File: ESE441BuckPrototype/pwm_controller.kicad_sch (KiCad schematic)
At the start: 56 parts, among them IC1 NCP81233MNTXG, J1 Header

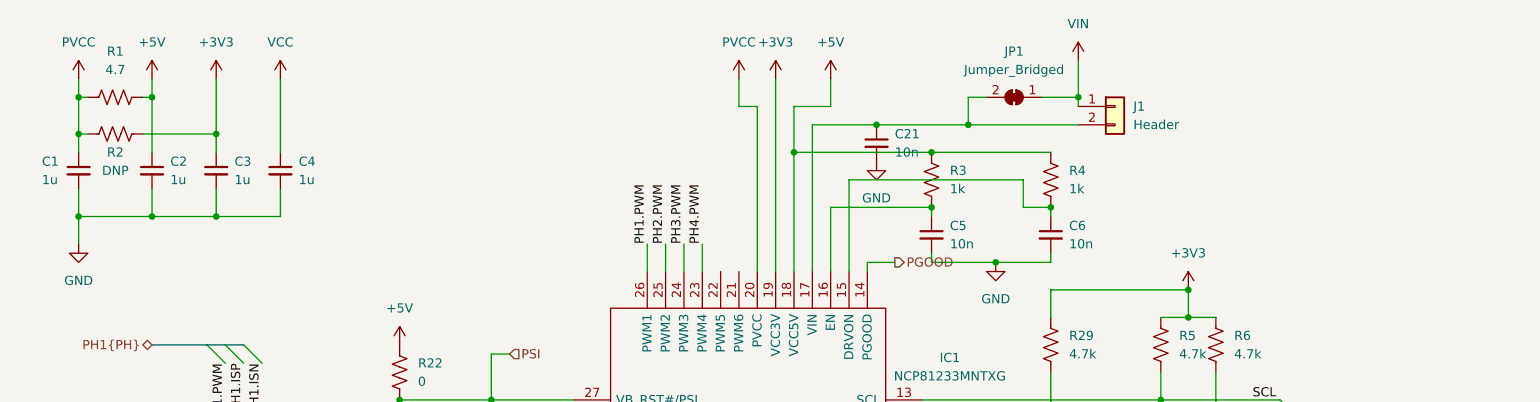
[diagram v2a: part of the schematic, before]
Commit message: Connect enable to MCU; Testpoints
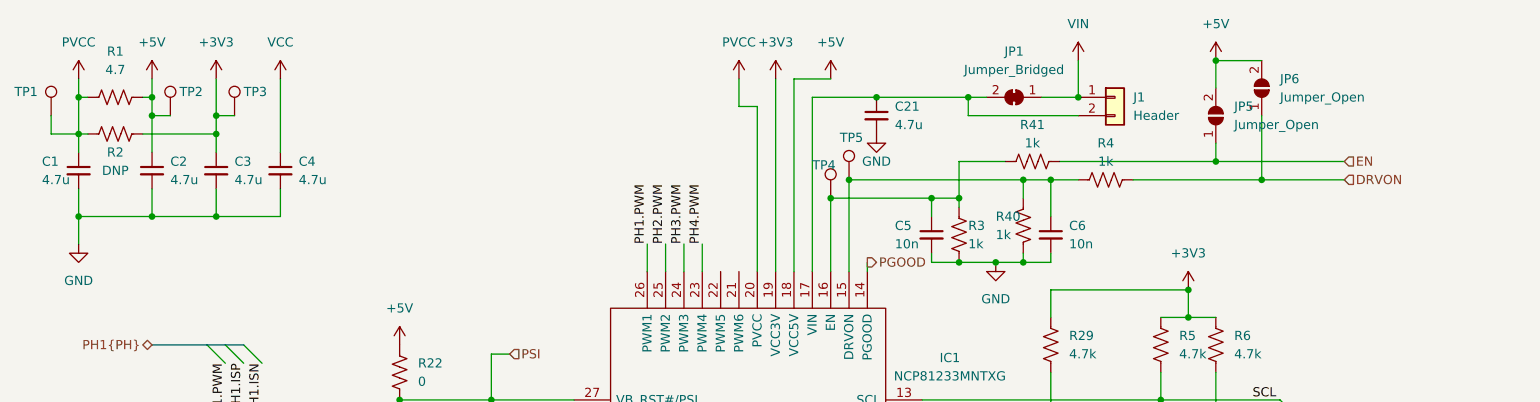
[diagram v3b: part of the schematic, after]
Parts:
- added JP5, JP6: Jumper_Open, symbol Jumper:SolderJumper_2_Open
- added R40, R41: 1k, Resistor_SMD:R_0603_1608Metric, symbol Device:R_US
- added TP1, TP2, TP3, TP4, TP5: TestPoint, TestPoint:TestPoint_Loop_D2.50mm_Drill1.0mm_LowProfile, symbol Connector:TestPoint
- C1, C2, C3, C4: value 1u -> 4.7u
- C21: value 10n -> 4.7u
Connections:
- net +3V3: now also TP3.1
- net +5V: now also JP5.2 (B), JP6.2 (B), TP2.1; no longer R3.1, R4.1
- net GND: now also R3.1, R40.2
- net PVCC: now also TP1.1
- net at C6.1, IC1.15 (DRVON), R4.2: now also R40.1, TP5.1
- net at C5.1, IC1.16 (EN), R3.2: now also R41.2, TP4.1
- new net DRVON: JP6.1 (A), R4.1
- new net EN: JP5.1 (A), R41.1
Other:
- moved on the sheet: C21, J1, R3, R4

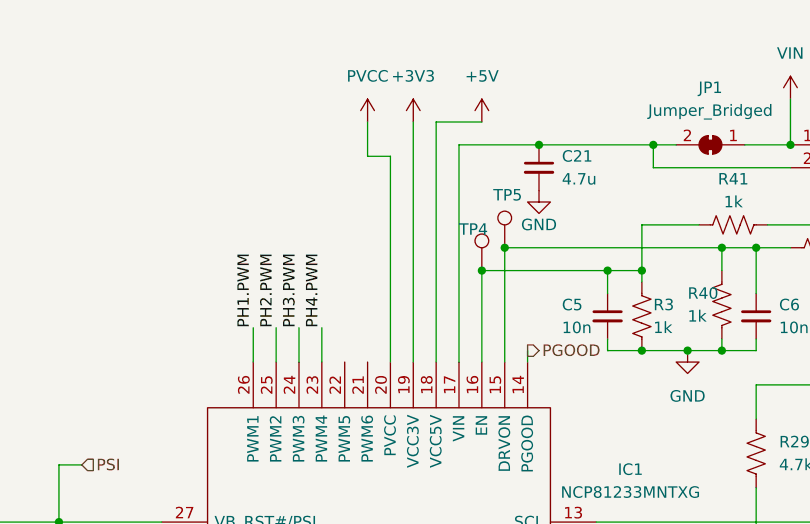
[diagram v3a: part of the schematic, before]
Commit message: Add openable jumper for internal 5V LDO
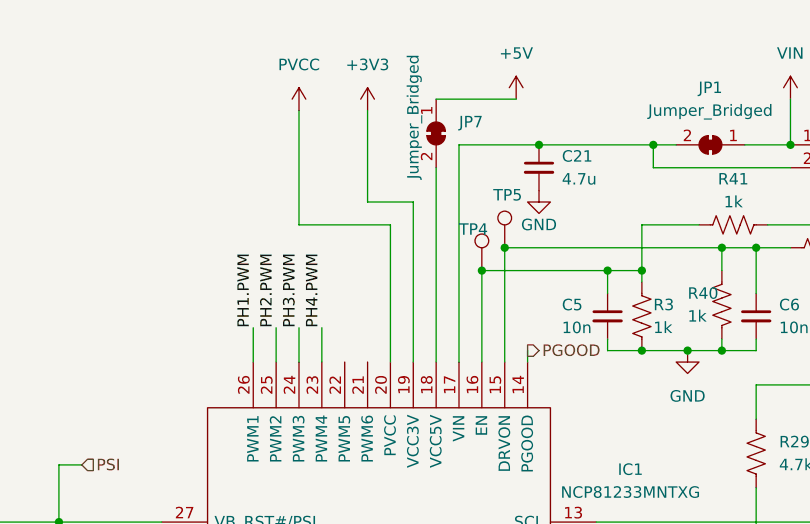
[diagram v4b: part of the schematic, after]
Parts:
- added JP7: Jumper_Bridged, symbol Jumper:SolderJumper_2_Bridged
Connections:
- net +5V: now also JP7.1 (A); no longer IC1.18 (VCC5V)
- new net: IC1.18 (VCC5V), JP7.2 (B)
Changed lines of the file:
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@@
-    (stroke (width 0) (type default) (color 0 0 0 0))
-  )
-  (wire (pts (xy 128.27 24.13) (xy 123.19 24.13))
     (stroke (width 0) (type default) (color 0 0 0 0))
   )
@@
     (stroke (width 0) (type default) (color 0 0 0 0))
   )
-  (wire (pts (xy 120.65 24.13) (xy 120.65 50.8))
-    (stroke (width 0) (type default) (color 0 0 0 0))
-  )
   (bus (pts (xy 193.04 71.12) (xy 195.58 71.12))
     (stroke (width 0) (type default) (color 0 0 0 0))
   )
+  (wire (pts (xy 115.57 22.86) (xy 115.57 33.02))
+    (stroke (width 0) (type default) (color 0 0 0 0))
+  )
   (wire (pts (xy 182.88 88.9) (xy 140.97 88.9))
     (stroke (width 0) (type default) (color 0 0 0 0))
@@
     (stroke (width 0) (type default) (color 0 0 0 0))
   )
+  (wire (pts (xy 118.11 35.56) (xy 107.95 35.56))
+    (stroke (width 0) (type default) (color 0 0 0 0))
+  )
   (wire (pts (xy 190.5 68.58) (xy 173.99 68.58))
     (stroke (width 0) (type default) (color 0 0 0 0))
@@
     (stroke (width 0) (type default) (color 0 0 0 0))
   )
+  (wire (pts (xy 107.95 35.56) (xy 107.95 22.86))
+    (stroke (width 0) (type default) (color 0 0 0 0))
+  )
   (wire (pts (xy 81.28 153.67) (xy 76.2 153.67))
     (stroke (width 0) (type default) (color 0 0 0 0))
@@
     (stroke (width 0) (type default) (color 0 0 0 0))
   )
-  (wire (pts (xy 115.57 24.13) (xy 115.57 27.94))
-    (stroke (width 0) (type default) (color 0 0 0 0))
-  )
   (wire (pts (xy 76.2 129.54) (xy 76.2 140.97))
     (stroke (width 0) (type default) (color 0 0 0 0))
@@
     (stroke (width 0) (type default) (color 0 0 0 0))
   )
+  (wire (pts (xy 123.19 21.59) (xy 132.08 21.59))
+    (stroke (width 0) (type default) (color 0 0 0 0))
+  )
+  (wire (pts (xy 115.57 33.02) (xy 120.65 33.02))
+    (stroke (width 0) (type default) (color 0 0 0 0))
+  )
   (bus (pts (xy 34.29 101.6) (xy 41.91 101.6))
     (stroke (width 0) (type default) (color 0 0 0 0))
@@
     (stroke (width 0) (type default) (color 0 0 0 0))
   )
+  (wire (pts (xy 120.65 33.02) (xy 120.65 50.8))
+    (stroke (width 0) (type default) (color 0 0 0 0))
+  )
   (wire (pts (xy 149.86 132.08) (xy 163.83 132.08))
     (stroke (width 0) (type default) (color 0 0 0 0))
@@
     (stroke (width 0) (type default) (color 0 0 0 0))
   )
+  (wire (pts (xy 123.19 29.21) (xy 123.19 50.8))
+    (stroke (width 0) (type default) (color 0 0 0 0))
+  )
   (wire (pts (xy 196.85 107.95) (xy 204.47 107.95))
     (stroke (width 0) (type default) (color 0 0 0 0))
@@
     (stroke (width 0) (type default) (color 0 0 0 0))
   )
-  (wire (pts (xy 118.11 27.94) (xy 118.11 50.8))
+  (wire (pts (xy 118.11 35.56) (xy 118.11 50.8))
     (stroke (width 0) (type default) (color 0 0 0 0))
   )
@@
     (stroke (width 0) (type default) (color 0 0 0 0))
   )
-  (wire (pts (xy 123.19 24.13) (xy 123.19 50.8))
-    (stroke (width 0) (type default) (color 0 0 0 0))
-  )
   (wire (pts (xy 182.88 107.95) (xy 189.23 107.95))
     (stroke (width 0) (type default) (color 0 0 0 0))
   )
   (wire (pts (xy 34.29 39.37) (xy 34.29 43.18))
-    (stroke (width 0) (type default) (color 0 0 0 0))
-  )
-  (wire (pts (xy 115.57 27.94) (xy 118.11 27.94))
     (stroke (width 0) (type default) (color 0 0 0 0))
   )
@@
     (pin "2")
   )
-  (symbol (lib_id "power:+5V") (at 128.27 24.13 0) (unit 1)
-    (in_bom yes) (on_board yes) (fields_autoplaced)
-    (property "Reference" "#PWR0118" (id 0) (at 128.27 27.94 0)
-      (effects (font (size 1.27 1.27)) hide)
-    )
-    (property "Value" "+5V" (id 1) (at 128.27 19.05 0))
-    (property "Footprint" "" (id 2) (at 128.27 24.13 0)
-      (effects (font (size 1.27 1.27)) hide)
-    )
-    (property "Datasheet" "" (id 3) (at 128.27 24.13 0)
+  (symbol (lib_id "power:+5V") (at 132.08 21.59 0) (unit 1)
+    (in_bom yes) (on_board yes) (fields_autoplaced)
+    (property "Reference" "#PWR0118" (id 0) (at 132.08 25.4 0)
+      (effects (font (size 1.27 1.27)) hide)
+    )
+    (property "Value" "+5V" (id 1) (at 132.08 16.51 0))
+    (property "Footprint" "" (id 2) (at 132.08 21.59 0)
+      (effects (font (size 1.27 1.27)) hide)
+    )
+    (property "Datasheet" "" (id 3) (at 132.08 21.59 0)
       (effects (font (size 1.27 1.27)) hide)
     )
@@
     )
     (pin "1")
+  )
+  (symbol (lib_id "Jumper:SolderJumper_2_Bridged") (at 123.19 25.4 90) (mirror x) (unit 1)
+    (in_bom yes) (on_board yes)
+    (property "Reference" "JP7" (id 0) (at 125.73 24.1299 90)
+      (effects (font (size 1.27 1.27)) (justify right))
+    )
+    (property "Value" "Jumper_Bridged" (id 1) (at 120.65 30.4799 0)
+      (effects (font (size 1.27 1.27)) (justify right))
+    )
+    (property "Footprint" "" (id 2) (at 123.19 25.4 0)
+      (effects (font (size 1.27 1.27)) hide)
+    )
+    (property "Datasheet" "~" (id 3) (at 123.19 25.4 0)
+      (effects (font (size 1.27 1.27)) hide)
+    )
+    (pin "1")
+    (pin "2")
   )
   (symbol (lib_id "power:+3V3") (at 177.8 53.34 0) (unit 1)
@@
     (pin "2")
   )
-  (symbol (lib_id "CustomPartsLibrary:PVCC") (at 115.57 24.13 0) (unit 1)
-    (in_bom yes) (on_board yes) (fields_autoplaced)
-    (property "Reference" "#PWR0117" (id 0) (at 115.57 27.94 0)
-      (effects (font (size 1.27 1.27)) hide)
-    )
-    (property "Value" "PVCC" (id 1) (at 115.57 19.05 0))
-    (property "Footprint" "" (id 2) (at 115.57 24.13 0)
-      (effects (font (size 1.27 1.27)) hide)
-    )
-    (property "Datasheet" "" (id 3) (at 115.57 24.13 0)
+  (symbol (lib_id "CustomPartsLibrary:PVCC") (at 107.95 22.86 0) (unit 1)
+    (in_bom yes) (on_board yes) (fields_autoplaced)
+    (property "Reference" "#PWR0117" (id 0) (at 107.95 26.67 0)
+      (effects (font (size 1.27 1.27)) hide)
+    )
+    (property "Value" "PVCC" (id 1) (at 107.95 17.78 0))
+    (property "Footprint" "" (id 2) (at 107.95 22.86 0)
+      (effects (font (size 1.27 1.27)) hide)
+    )
+    (property "Datasheet" "" (id 3) (at 107.95 22.86 0)
       (effects (font (size 1.27 1.27)) hide)
     )
@@
     (pin "2")
   )
-  (symbol (lib_id "power:+3V3") (at 120.65 24.13 0) (unit 1)
-    (in_bom yes) (on_board yes) (fields_autoplaced)
-    (property "Reference" "#PWR0116" (id 0) (at 120.65 27.94 0)
-      (effects (font (size 1.27 1.27)) hide)
-    )
-    (property "Value" "+3V3" (id 1) (at 120.65 19.05 0))
-    (property "Footprint" "" (id 2) (at 120.65 24.13 0)
-      (effects (font (size 1.27 1.27)) hide)
-    )
-    (property "Datasheet" "" (id 3) (at 120.65 24.13 0)
-      (effects (font (size 1.27 1.27)) hide)
-    )
+  (symbol (lib_id "power:+3V3") (at 115.57 22.86 0) (unit 1)
+    (in_bom yes) (on_board yes) (fields_autoplaced)
+    (property "Reference" "#PWR0116" (id 0) (at 115.57 26.67 0)
+      (effects (font (size 1.27 1.27)) hide)
+    )
+    (property "Value" "+3V3" (id 1) (at 115.57 17.78 0))
+    (property "Footprint" "" (id 2) (at 115.57 22.86 0)
+      (effects (font (size 1.27 1.27)) hide)
+    )
+    (property "Datasheet" "" (id 3) (at 115.57 22.86 0)
+      (effects (font (size 1.27 1.27)) hide)
+    )
